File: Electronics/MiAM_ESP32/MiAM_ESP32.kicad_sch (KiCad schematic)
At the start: 22 parts, among them J1 Conn_01x06_Male, J10 Conn_01x03_Male, J11 Conn_01x02_Male, J12 Conn_01x02_Male, J13 Conn_01x02_Male, J14 Conn_01x02_Male, J2 Conn_01x06_Male, J3 Screw_Terminal_01x02, J4 Conn_01x03_Male, J5 Conn_01x06_Male, J6 Conn_01x04_Male, J7 Conn_01x02_Male, J8 Conn_01x04_Male, J9 Conn_01x03_Male, SW1 SW_Push, U1 ESP32-DEVKIT-V1, U2 L293D, U3 XL6009_DC-DC, U5 LM7805_TO220

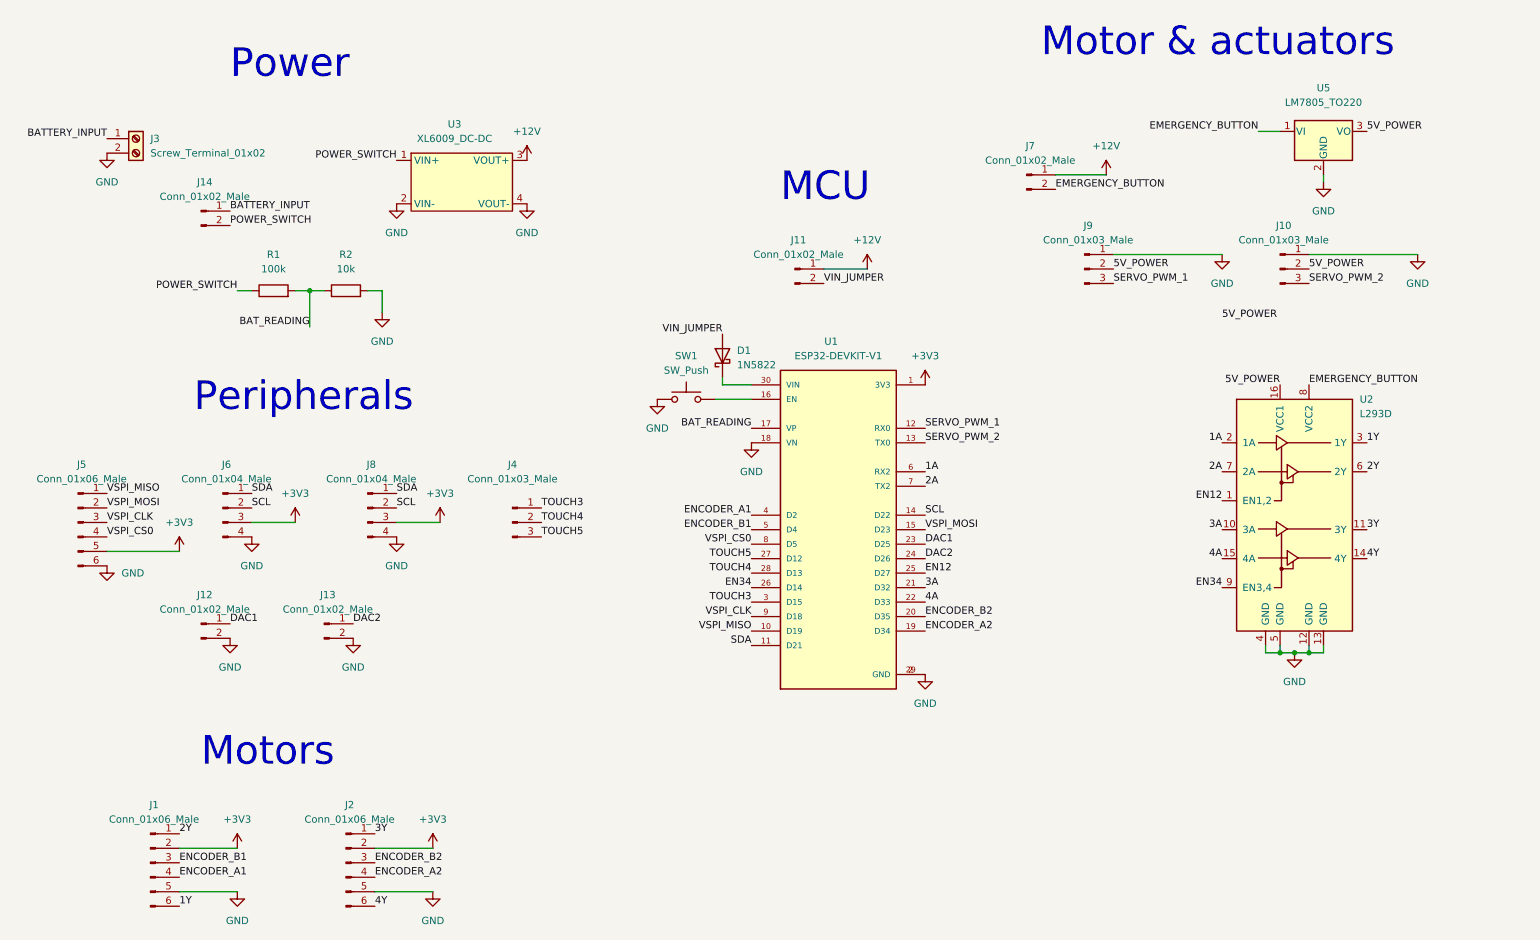
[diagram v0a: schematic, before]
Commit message: Make more condensed version of pcb
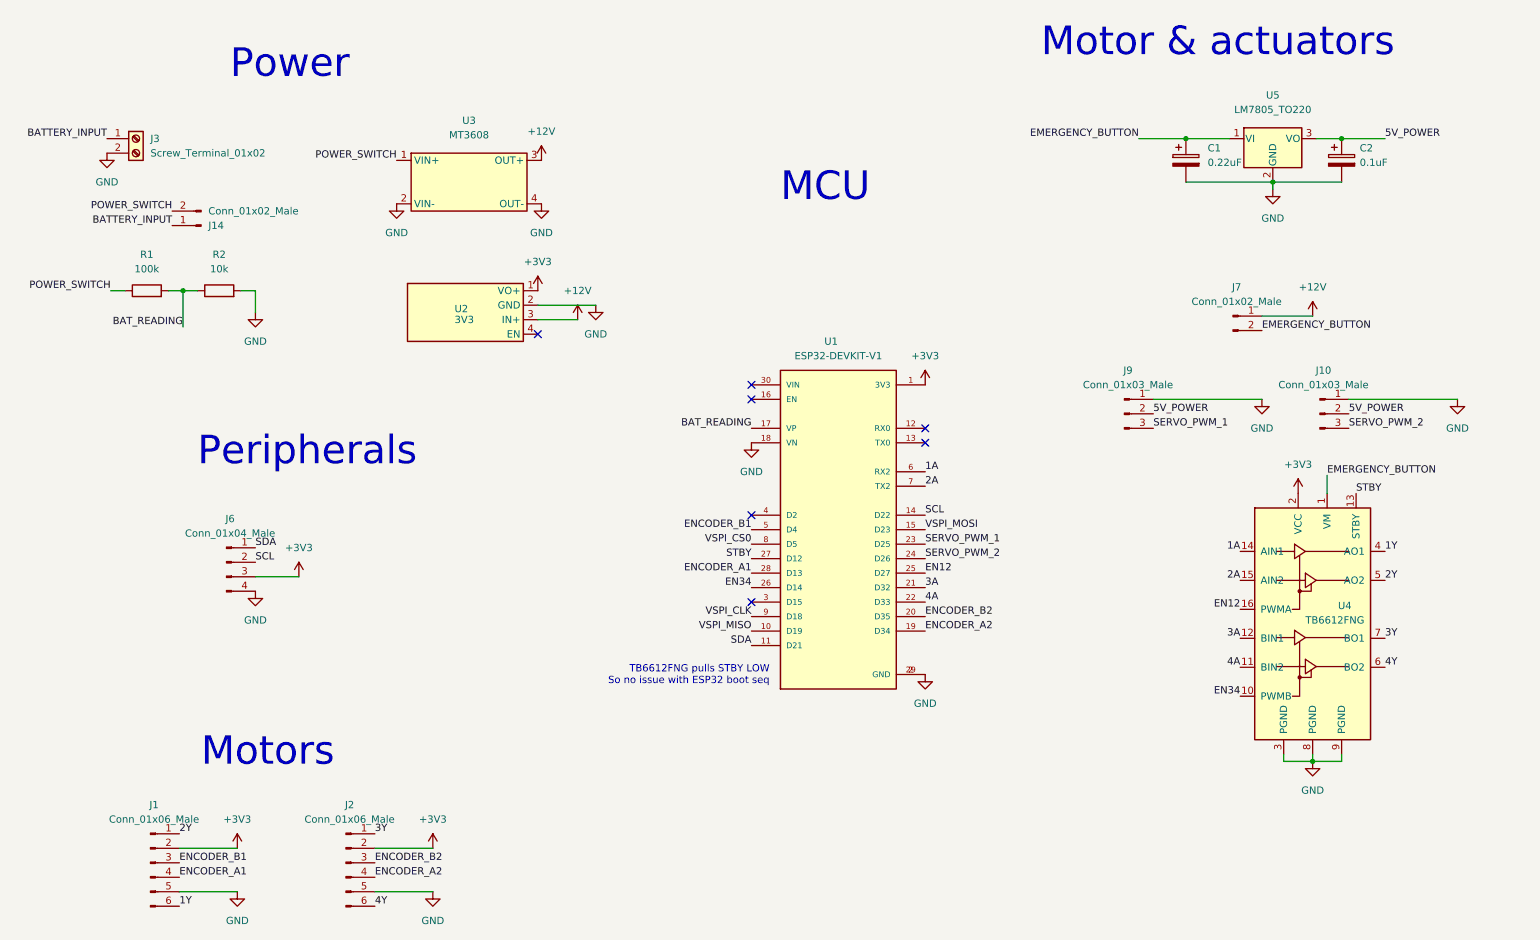
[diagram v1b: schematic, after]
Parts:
- removed D1: 1N5822, Diode_THT:D_DO-201AD_P15.24mm_Horizontal, symbol Diode:1N5822
- removed J11, J12, J13: Conn_01x02_Male, Connector_PinHeader_2.54mm:PinHeader_1x02_P2.54mm_Vertical, symbol Connector:Conn_01x02_Male
- removed J4: Conn_01x03_Male, Connector_PinHeader_2.54mm:PinHeader_1x03_P2.54mm_Vertical, symbol Connector:Conn_01x03_Male
- removed J5: Conn_01x06_Male, Connector_PinHeader_2.54mm:PinHeader_1x06_P2.54mm_Vertical, symbol Connector:Conn_01x06_Male
- removed J8: Conn_01x04_Male, Connector_PinHeader_2.54mm:PinHeader_1x04_P2.54mm_Vertical, symbol Connector:Conn_01x04_Male
- removed SW1: SW_Push, Button_Switch_SMD:SW_Push_1P1T_NO_Vertical_Wuerth_434133025816, symbol Switch:SW_Push
- removed U2: L293D, Package_DIP:DIP-16_W7.62mm, symbol Driver_Motor:L293D
- removed U3: XL6009_DC-DC, MiAM_ESP32_Footprints:XL6009_DCDC, symbol MiAM_ESP32:XL6009_DC-DC
- added C1: 0.22uF, Capacitor_THT:CP_Radial_D4.0mm_P2.00mm, symbol Device:C_Polarized
- added C2: 0.1uF, Capacitor_THT:CP_Radial_Tantal_D5.0mm_P5.00mm, symbol Device:C_Polarized
- added U2: 3V3, MiAM_ESP32_Footprints:VoltageRegulator, symbol MiAM_ESP32:VoltageRegulator
- added U3: MT3608, MiAM_ESP32_Footprints:MT3608, symbol MiAM_ESP32:MT3608
- added U4: TB6612FNG, MiAM_ESP32_Footprints:TB6612FNG, symbol MiAM_ESP32:TB6612FNG
- J3: footprint TerminalBlock_MetzConnect:TerminalBlock_MetzConnect_Type011_RT05502HBWC_1x02_P5.00mm_Horizontal -> Connector_JST:JST_PH_B2B-PH-K_1x02_P2.00mm_Vertical
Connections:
- net DAC1 is gone; now on net SERVO_PWM_1: U1.23 (D25)
- net DAC2 is gone; now on net SERVO_PWM_2: U1.24 (D26)
- net TOUCH4 is gone; now on net ENCODER_A1: U1.28 (D13)
- net +12V: now also U2.3 (IN+), U3.3 (OUT+)
- net +3V3: now also U2.1 (VO+), U4.2 (VCC)
- net 1A: now also U4.14 (AIN1)
- net 1Y: now also U4.4 (AO1)
- net 2A: now also U4.15 (AIN2)
- net 2Y: now also U4.5 (AO2)
- net 3A: now also U4.12 (BIN1)
- net 3Y: now also U4.7 (BO1)
- net 4A: now also U4.11 (BIN2)
- net 4Y: now also U4.6 (BO2)
- net 5V_POWER: now also C2.1
- net EMERGENCY_BUTTON: now also C1.1, U4.1 (VM)
- net EN12: now also U4.16 (PWMA)
- net EN34: now also U4.10 (PWMB)
- net ENCODER_A1: no longer U1.4 (D2)
- net GND: now also C1.2, C2.2, U2.2 (GND), U3.2 (VIN-), U3.4 (OUT-), U4.3 (PGND), U4.8 (PGND), U4.9 (PGND)
- net POWER_SWITCH: now also U3.1 (VIN+)
- net SERVO_PWM_1: no longer U1.12 (RX0)
- net SERVO_PWM_2: no longer U1.13 (TX0)
- net TOUCH3: no longer names the net of U1.3 (D15)
- net TOUCH5 renamed STBY
- net STBY: now also U4.13 (STBY)
- no-connect marks 0 -> 7
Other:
- note added: "TB6612FNG pulls STBY LOW So no issue with ESP32 boot seq"
- moved on the sheet: J10, J14, J6, J7, J9, R1, R2, U5

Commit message: Fix initial PAMI pcb
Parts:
- added D1: D_Schottky, Diode_THT:D_DO-41_SOD81_P7.62mm_Horizontal, symbol Device:D_Schottky
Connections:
- net +3V3: now also D1.2 (A); no longer U1.1 (3V3)
- new net: D1.1 (K), U1.1 (3V3)
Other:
- note added: "Pin 2 is internal LED"
- note added: "Pins not to use : RX0, TX0 Pins which should not be pulled high (at startup): 2, 12 Pins which output PWM at startup: 5, 14, 15 Pins input only: 34, 35, 36, 39"
- note added: "Servomotors"
- note added: "TB6612FNG pulls STBY low So no issue with ESP32 boot seq"
- note removed: "Motor & actuators"
- note removed: "Peripherals"
- note removed: "TB6612FNG pulls STBY LOW So no issue with ESP32 boot seq"
- moved on the sheet: C1, C2, J1, J10, J14, J2, J3, J6, J7, J9, R1, R2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
